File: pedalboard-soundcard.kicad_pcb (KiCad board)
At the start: 2 copper layers, 65 x 56 mm, 76 parts, among them J1 RPi_GPIO, J2 Conn_02x03_Odd_Even, J3 Conn_02x03_Odd_Even, U1 AT24CS01-STUM, U2 NCP163, U3 NCP163, U4 PCM1863DBT, U5 NCP163, U6 PCM5242RHBR, X1 22.5792Mhz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

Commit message: Replace 5v global label with +5V power
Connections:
- net 5v renamed +5V
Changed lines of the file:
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@@
   (net 18 "unconnected-(J1-BCM24-Pad18)")
   (net 19 "unconnected-(J1-BCM10_MOSI-Pad19)")
-  (net 20 "5v")
+  (net 20 "+5V")
   (net 21 "unconnected-(J1-BCM9_MISO-Pad21)")
   (net 22 "unconnected-(J1-BCM25-Pad22)")
@@
       (net 1 "unconnected-(J1-3.3V-Pad1)") (pinfunction "3.3V") (pintype "power_in+no_connect"))
     (pad "2" thru_hole oval locked (at 1.27 -24.13 90) (size 1.7272 1.7272) (drill 1.016) (layers "*.Cu" "*.Mask")
-      (net 20 "5v") (pinfunction "5V") (pintype "power_in"))
+      (net 20 "+5V") (pinfunction "5V") (pintype "power_in"))
     (pad "3" thru_hole oval locked (at -1.27 -21.59 90) (size 1.7272 1.7272) (drill 1.016) (layers "*.Cu" "*.Mask")
       (net 47 "sda") (pinfunction "BCM2_SDA") (pintype "bidirectional"))
     (pad "4" thru_hole oval locked (at 1.27 -21.59 90) (size 1.7272 1.7272) (drill 1.016) (layers "*.Cu" "*.Mask")
-      (net 20 "5v") (pinfunction "5V") (pintype "power_in"))
+      (net 20 "+5V") (pinfunction "5V") (pintype "power_in"))
     (pad "5" thru_hole oval locked (at -1.27 -19.05 90) (size 1.7272 1.7272) (drill 1.016) (layers "*.Cu" "*.Mask")
       (net 48 "scl") (pinfunction "BCM3_SCL") (pintype "bidirectional"))
@@
       (stroke (width 0.1) (type solid)) (layer "F.Fab"))
     (pad "1" smd roundrect (at -1.1375 -0.95 270) (size 1.325 0.6) (layers "F.Cu" "F.Paste" "F.Mask") (roundrect_rratio 0.25)
-      (net 20 "5v") (pinfunction "IN") (pintype "power_in"))
+      (net 20 "+5V") (pinfunction "IN") (pintype "power_in"))
     (pad "2" smd roundrect (at -1.1375 0 270) (size 1.325 0.6) (layers "F.Cu" "F.Paste" "F.Mask") (roundrect_rratio 0.25)
       (net 2 "GND") (pinfunction "GND") (pintype "power_in"))
     (pad "3" smd roundrect (at -1.1375 0.95 270) (size 1.325 0.6) (layers "F.Cu" "F.Paste" "F.Mask") (roundrect_rratio 0.25)
-      (net 20 "5v") (pinfunction "EN") (pintype "input"))
+      (net 20 "+5V") (pinfunction "EN") (pintype "input"))
     (pad "4" smd roundrect (at 1.1375 0.95 270) (size 1.325 0.6) (layers "F.Cu" "F.Paste" "F.Mask") (roundrect_rratio 0.25)
       (net 76 "unconnected-(U2-NC-Pad4)") (pinfunction "NC") (pintype "no_connect"))
@@
       (stroke (width 0.1) (type solid)) (layer "F.Fab"))
     (pad "1" smd roundrect (at -0.95 0 180) (size 1 1.45) (layers "F.Cu" "F.Paste" "F.Mask") (roundrect_rratio 0.25)
-      (net 20 "5v") (pintype "passive"))
+      (net 20 "+5V") (pintype "passive"))
     (pad "2" smd roundrect (at 0.95 0 180) (size 1 1.45) (layers "F.Cu" "F.Paste" "F.Mask") (roundrect_rratio 0.25)
       (net 2 "GND") (pintype "passive"))
@@
       (stroke (width 0.1) (type solid)) (layer "F.Fab"))
     (pad "1" smd roundrect (at -1.1375 -0.95 270) (size 1.325 0.6) (layers "F.Cu" "F.Paste" "F.Mask") (roundrect_rratio 0.25)
-      (net 20 "5v") (pinfunction "IN") (pintype "power_in"))
+      (net 20 "+5V") (pinfunction "IN") (pintype "power_in"))
     (pad "2" smd roundrect (at -1.1375 0 270) (size 1.325 0.6) (layers "F.Cu" "F.Paste" "F.Mask") (roundrect_rratio 0.25)
       (net 2 "GND") (pinfunction "GND") (pintype "power_in"))
     (pad "3" smd roundrect (at -1.1375 0.95 270) (size 1.325 0.6) (layers "F.Cu" "F.Paste" "F.Mask") (roundrect_rratio 0.25)
-      (net 20 "5v") (pinfunction "EN") (pintype "input"))
+      (net 20 "+5V") (pinfunction "EN") (pintype "input"))
     (pad "4" smd roundrect (at 1.1375 0.95 270) (size 1.325 0.6) (layers "F.Cu" "F.Paste" "F.Mask") (roundrect_rratio 0.25)
       (net 78 "unconnected-(U5-NC-Pad4)") (pinfunction "NC") (pintype "no_connect"))
@@
       (stroke (width 0.1) (type solid)) (layer "F.Fab"))
     (pad "1" smd roundrect (at -0.95 0 180) (size 1 1.45) (layers "F.Cu" "F.Paste" "F.Mask") (roundrect_rratio 0.25)
-      (net 20 "5v") (pintype "passive"))
+      (net 20 "+5V") (pintype "passive"))
     (pad "2" smd roundrect (at 0.95 0 180) (size 1 1.45) (layers "F.Cu" "F.Paste" "F.Mask") (roundrect_rratio 0.25)
       (net 2 "GND") (pintype "passive"))
@@
       (stroke (width 0.1) (type solid)) (layer "F.Fab"))
     (pad "1" smd roundrect (at -1.1375 -0.95 270) (size 1.325 0.6) (layers "F.Cu" "F.Paste" "F.Mask") (roundrect_rratio 0.25)
-      (net 20 "5v") (pinfunction "IN") (pintype "power_in"))
+      (net 20 "+5V") (pinfunction "IN") (pintype "power_in"))
     (pad "2" smd roundrect (at -1.1375 0 270) (size 1.325 0.6) (layers "F.Cu" "F.Paste" "F.Mask") (roundrect_rratio 0.25)
       (net 2 "GND") (pinfunction "GND") (pintype "power_in"))
     (pad "3" smd roundrect (at -1.1375 0.95 270) (size 1.325 0.6) (layers "F.Cu" "F.Paste" "F.Mask") (roundrect_rratio 0.25)
-      (net 20 "5v") (pinfunction "EN") (pintype "input"))
+      (net 20 "+5V") (pinfunction "EN") (pintype "input"))
     (pad "4" smd roundrect (at 1.1375 0.95 270) (size 1.325 0.6) (layers "F.Cu" "F.Paste" "F.Mask") (roundrect_rratio 0.25)
       (net 77 "unconnected-(U3-NC-Pad4)") (pinfunction "NC") (pintype "no_connect"))
@@
       (stroke (width 0.1) (type solid)) (layer "F.Fab"))
     (pad "1" smd roundrect (at -0.95 0) (size 1 1.45) (layers "F.Cu" "F.Paste" "F.Mask") (roundrect_rratio 0.25)
-      (net 20 "5v") (pintype "passive"))
+      (net 20 "+5V") (pintype "passive"))
     (pad "2" smd roundrect (at 0.95 0) (size 1 1.45) (layers "F.Cu" "F.Paste" "F.Mask") (roundrect_rratio 0.25)
       (net 2 "GND") (pintype "passive"))

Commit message: Replace DVDD global label with VDD power symbol
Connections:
- net DVDD renamed VDD
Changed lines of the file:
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@@
   (net 1 "unconnected-(J1-3.3V-Pad1)")
   (net 2 "GND")
-  (net 3 "DVDD")
+  (net 3 "VDD")
   (net 4 "Net-(C2-Pad1)")
   (net 5 "/ADC/inr+")
@@
       (net 73 "Net-(X1-OUT)") (pinfunction "OUT") (pintype "output"))
     (pad "4" smd rect (at -0.825 -0.775 90) (size 0.65 0.85) (layers "F.Cu" "F.Paste" "F.Mask")
-      (net 3 "DVDD") (pinfunction "VDD") (pintype "power_in"))
+      (net 3 "VDD") (pinfunction "VDD") (pintype "power_in"))
     (model "${KICAD6_3DMODEL_DIR}/Oscillator.3dshapes/Oscillator_SMD_Abracon_ASDMB-4Pin_2.5x2.0mm.wrl"
       (offset (xyz 0 0 0))
@@
       (net 76 "unconnected-(U2-NC-Pad4)") (pinfunction "NC") (pintype "no_connect"))
     (pad "5" smd roundrect (at 1.1375 -0.95 270) (size 1.325 0.6) (layers "F.Cu" "F.Paste" "F.Mask") (roundrect_rratio 0.25)
-      (net 3 "DVDD") (pinfunction "OUT") (pintype "power_out"))
+      (net 3 "VDD") (pinfunction "OUT") (pintype "power_out"))
     (model "${KICAD6_3DMODEL_DIR}/Package_TO_SOT_SMD.3dshapes/SOT-23-5.wrl"
       (offset (xyz 0 0 0))
@@
       (stroke (width 0.1) (type solid)) (layer "F.Fab"))
     (pad "1" smd roundrect (at -0.95 0 90) (size 1 1.45) (layers "F.Cu" "F.Paste" "F.Mask") (roundrect_rratio 0.25)
-      (net 3 "DVDD") (pintype "passive"))
+      (net 3 "VDD") (pintype "passive"))
     (pad "2" smd roundrect (at 0.95 0 90) (size 1 1.45) (layers "F.Cu" "F.Paste" "F.Mask") (roundrect_rratio 0.25)
       (net 2 "GND") (pintype "passive"))
@@
       (stroke (width 0.1) (type solid)) (layer "F.Fab"))
     (pad "1" smd roundrect (at -0.95 0) (size 1 1.45) (layers "F.Cu" "F.Paste" "F.Mask") (roundrect_rratio 0.25)
-      (net 3 "DVDD") (pintype "passive"))
+      (net 3 "VDD") (pintype "passive"))
     (pad "2" smd roundrect (at 0.95 0) (size 1 1.45) (layers "F.Cu" "F.Paste" "F.Mask") (roundrect_rratio 0.25)
       (net 2 "GND") (pintype "passive"))
@@
       (net 51 "/ID_SC") (pintype "passive"))
     (pad "2" smd roundrect (at 0.9125 0) (size 1.025 1.4) (layers "F.Cu" "F.Paste" "F.Mask") (roundrect_rratio 0.243902)
-      (net 3 "DVDD") (pintype "passive"))
+      (net 3 "VDD") (pintype "passive"))
     (model "${KICAD6_3DMODEL_DIR}/Resistor_SMD.3dshapes/R_0805_2012Metric.wrl"
       (offset (xyz 0 0 0))
@@
       (stroke (width 0.1) (type solid)) (layer "F.Fab"))
     (pad "1" smd roundrect (at -0.9125 0) (size 1.025 1.4) (layers "F.Cu" "F.Paste" "F.Mask") (roundrect_rratio 0.243902)
-      (net 3 "DVDD") (pintype "passive"))
+      (net 3 "VDD") (pintype "passive"))
     (pad "2" smd roundrect (at 0.9125 0) (size 1.025 1.4) (layers "F.Cu" "F.Paste" "F.Mask") (roundrect_rratio 0.243902)
       (net 58 "Net-(U1-WP)") (pintype "passive"))
@@
       (net 75 "Net-(X2-OUT)") (pinfunction "OUT") (pintype "output"))
     (pad "4" smd rect (at -0.825 -0.775 90) (size 0.65 0.85) (layers "F.Cu" "F.Paste" "F.Mask")
-      (net 3 "DVDD") (pinfunction "VDD") (pintype "power_in"))
+      (net 3 "VDD") (pinfunction "VDD") (pintype "power_in"))
     (model "${KICAD6_3DMODEL_DIR}/Oscillator.3dshapes/Oscillator_SMD_Abracon_ASDMB-4Pin_2.5x2.0mm.wrl"
       (offset (xyz 0 0 0))
@@
       (net 2 "GND") (pintype "passive"))
     (pad "2" smd roundrect (at 0.95 0 90) (size 1 1.45) (layers "F.Cu" "F.Paste" "F.Mask") (roundrect_rratio 0.25)
-      (net 3 "DVDD") (pintype "passive"))
+      (net 3 "VDD") (pintype "passive"))
     (model "${KICAD6_3DMODEL_DIR}/Capacitor_SMD.3dshapes/C_0805_2012Metric.wrl"
       (offset (xyz 0 0 0))
@@
       (stroke (width 0.1) (type solid)) (layer "F.Fab"))
     (pad "1" smd roundrect (at -0.95 0 180) (size 1 1.45) (layers "F.Cu" "F.Paste" "F.Mask") (roundrect_rratio 0.25)
-      (net 3 "DVDD") (pintype "passive"))
+      (net 3 "VDD") (pintype "passive"))
     (pad "2" smd roundrect (at 0.95 0 180) (size 1 1.45) (layers "F.Cu" "F.Paste" "F.Mask") (roundrect_rratio 0.25)
       (net 2 "GND") (pintype "passive"))
@@
       (net 2 "GND") (pinfunction "DGND") (pintype "power_in"))
     (pad "4" smd roundrect (at -2.4375 -0.25 90) (size 0.875 0.25) (layers "F.Cu" "F.Paste" "F.Mask") (roundrect_rratio 0.25)
-      (net 3 "DVDD") (pinfunction "DVDD") (pintype "power_in"))
+      (net 3 "VDD") (pinfunction "DVDD") (pintype "power_in"))
     (pad "5" smd roundrect (at -2.4375 0.25 90) (size 0.875 0.25) (layers "F.Cu" "F.Paste" "F.Mask") (roundrect_rratio 0.25)
-      (net 3 "DVDD") (pinfunction "CPVDD") (pintype "power_in"))
+      (net 3 "VDD") (pinfunction "CPVDD") (pintype "power_in"))
     (pad "6" smd roundrect (at -2.4375 0.75 90) (size 0.875 0.25) (layers "F.Cu" "F.Paste" "F.Mask") (roundrect_rratio 0.25)
       (net 46 "Net-(U6-CAPP)") (pinfunction "CAPP") (pintype "output"))
@@
       (net 2 "GND") (pinfunction "DGND") (pintype "power_in"))
     (pad "13" smd roundrect (at -2.8625 2.5 180) (size 1.475 0.3) (layers "F.Cu" "F.Paste" "F.Mask") (roundrect_rratio 0.25)
-      (net 3 "DVDD") (pinfunction "DVDD") (pintype "power_in"))
+      (net 3 "VDD") (pinfunction "DVDD") (pintype "power_in"))
     (pad "14" smd roundrect (at -2.8625 3 180) (size 1.475 0.3) (layers "F.Cu" "F.Paste" "F.Mask") (roundrect_rratio 0.25)
-      (net 3 "DVDD") (pinfunction "IOVDD") (pintype "power_in"))
+      (net 3 "VDD") (pinfunction "IOVDD") (pintype "power_in"))
     (pad "15" smd roundrect (at -2.8625 3.5 180) (size 1.475 0.3) (layers "F.Cu" "F.Paste" "F.Mask") (roundrect_rratio 0.25)
       (net 74 "master_clk") (pinfunction "SCKI") (pintype "input"))
@@
       (net 2 "GND") (pintype "passive"))
     (pad "2" smd roundrect (at 0.95 0 90) (size 1 1.45) (layers "F.Cu" "F.Paste" "F.Mask") (roundrect_rratio 0.25)
-      (net 3 "DVDD") (pintype "passive"))
+      (net 3 "VDD") (pintype "passive"))
     (model "${KICAD6_3DMODEL_DIR}/Capacitor_SMD.3dshapes/C_0805_2012Metric.wrl"
       (offset (xyz 0 0 0))
@@
       (net 2 "GND") (pintype "passive"))
     (pad "2" smd roundrect (at 0.95 0 90) (size 1 1.45) (layers "F.Cu" "F.Paste" "F.Mask") (roundrect_rratio 0.25)
-      (net 3 "DVDD") (pintype "passive"))
+      (net 3 "VDD") (pintype "passive"))
     (model "${KICAD6_3DMODEL_DIR}/Capacitor_SMD.3dshapes/C_0805_2012Metric.wrl"
       (offset (xyz 0 0 0))
@@
       (net 67 "Net-(U6-ADR1)") (pintype "passive"))
     (pad "2" smd roundrect (at 0.9125 0 180) (size 1.025 1.4) (layers "F.Cu" "F.Paste" "F.Mask") (roundrect_rratio 0.243902)
-      (net 3 "DVDD") (pintype "passive"))
+      (net 3 "VDD") (pintype "passive"))
     (model "${KICAD6_3DMODEL_DIR}/Resistor_SMD.3dshapes/R_0805_2012Metric.wrl"
       (offset (xyz 0 0 0))
@@
       (net 50 "/ID_SD") (pintype "passive"))
     (pad "2" smd roundrect (at 0.9125 0) (size 1.025 1.4) (layers "F.Cu" "F.Paste" "F.Mask") (roundrect_rratio 0.243902)
-      (net 3 "DVDD") (pintype "passive"))
+      (net 3 "VDD") (pintype "passive"))
     (model "${KICAD6_3DMODEL_DIR}/Resistor_SMD.3dshapes/R_0805_2012Metric.wrl"
       (offset (xyz 0 0 0))
@@
       (net 50 "/ID_SD") (pinfunction "SDA") (pintype "bidirectional"))
     (pad "4" smd roundrect (at 1.1375 0.95 180) (size 1.325 0.6) (layers "F.Cu" "F.Paste" "F.Mask") (roundrect_rratio 0.25)
-      (net 3 "DVDD") (pinfunction "VCC") (pintype "power_in"))
+      (net 3 "VDD") (pinfunction "VCC") (pintype "power_in"))
     (pad "5" smd roundrect (at 1.1375 -0.95 180) (size 1.325 0.6) (layers "F.Cu" "F.Paste" "F.Mask") (roundrect_rratio 0.25)
       (net 58 "Net-(U1-WP)") (pinfunction "WP") (pintype "input"))
@@
       (stroke (width 0.1) (type solid)) (layer "F.Fab"))
     (pad "1" smd roundrect (at -0.95 0 90) (size 1 1.45) (layers "F.Cu" "F.Paste" "F.Mask") (roundrect_rratio 0.25)
-      (net 3 "DVDD") (pintype "passive"))
+      (net 3 "VDD") (pintype "passive"))
     (pad "2" smd roundrect (at 0.95 0 90) (size 1 1.45) (layers "F.Cu" "F.Paste" "F.Mask") (roundrect_rratio 0.25)
       (net 2 "GND") (pintype "passive"))

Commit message: Use Power Symbols for analog power
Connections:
- net AVDD renamed VDDA
- net AVDD2 renamed VDDF
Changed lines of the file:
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@@
   (net 26 "unconnected-(J1-BCM7_CE1-Pad26)")
   (net 27 "/ADC/inl+")
-  (net 28 "AVDD2")
+  (net 28 "VDDF")
   (net 29 "unconnected-(J1-BCM5-Pad29)")
   (net 30 "Net-(U4-LDO)")
@@
   (net 32 "unconnected-(J1-BCM12_PWM0-Pad32)")
   (net 33 "unconnected-(J1-BCM13_PWM1-Pad33)")
-  (net 34 "AVDD")
+  (net 34 "VDDA")
   (net 35 "Net-(U4-VREF)")
   (net 36 "unconnected-(J1-BCM16-Pad36)")
@@
       (stroke (width 0.1) (type solid)) (layer "F.Fab"))
     (pad "1" smd roundrect (at -0.95 0) (size 1 1.45) (layers "F.Cu" "F.Paste" "F.Mask") (roundrect_rratio 0.25)
-      (net 28 "AVDD2") (pintype "passive"))
+      (net 28 "VDDF") (pintype "passive"))
     (pad "2" smd roundrect (at 0.95 0) (size 1 1.45) (layers "F.Cu" "F.Paste" "F.Mask") (roundrect_rratio 0.25)
       (net 2 "GND") (pintype "passive"))
@@
       (net 2 "GND") (pintype "passive"))
     (pad "2" smd roundrect (at 0.95 0 180) (size 1 1.45) (layers "F.Cu" "F.Paste" "F.Mask") (roundrect_rratio 0.25)
-      (net 34 "AVDD") (pintype "passive"))
+      (net 34 "VDDA") (pintype "passive"))
     (model "${KICAD6_3DMODEL_DIR}/Capacitor_SMD.3dshapes/C_0805_2012Metric.wrl"
       (offset (xyz 0 0 0))
@@
       (net 66 "Net-(U6-OUTRP)") (pinfunction "OUTRP") (pintype "output"))
     (pad "14" smd roundrect (at 0.75 2.4375 90) (size 0.25 0.875) (layers "F.Cu" "F.Paste" "F.Mask") (roundrect_rratio 0.25)
-      (net 34 "AVDD") (pinfunction "AVDD") (pintype "power_in"))
+      (net 34 "VDDA") (pinfunction "AVDD") (pintype "power_in"))
     (pad "15" smd roundrect (at 1.25 2.4375 90) (size 0.25 0.875) (layers "F.Cu" "F.Paste" "F.Mask") (roundrect_rratio 0.25)
       (net 2 "GND") (pinfunction "AGND") (pintype "power_in"))
@@
       (net 78 "unconnected-(U5-NC-Pad4)") (pinfunction "NC") (pintype "no_connect"))
     (pad "5" smd roundrect (at 1.1375 -0.95 270) (size 1.325 0.6) (layers "F.Cu" "F.Paste" "F.Mask") (roundrect_rratio 0.25)
-      (net 34 "AVDD") (pinfunction "OUT") (pintype "power_out"))
+      (net 34 "VDDA") (pinfunction "OUT") (pintype "power_out"))
     (model "${KICAD6_3DMODEL_DIR}/Package_TO_SOT_SMD.3dshapes/SOT-23-5.wrl"
       (offset (xyz 0 0 0))
@@
       (stroke (width 0.1) (type solid)) (layer "F.Fab"))
     (pad "1" smd roundrect (at -0.95 0) (size 1 1.45) (layers "F.Cu" "F.Paste" "F.Mask") (roundrect_rratio 0.25)
-      (net 34 "AVDD") (pintype "passive"))
+      (net 34 "VDDA") (pintype "passive"))
     (pad "2" smd roundrect (at 0.95 0) (size 1 1.45) (layers "F.Cu" "F.Paste" "F.Mask") (roundrect_rratio 0.25)
       (net 2 "GND") (pintype "passive"))
@@
       (stroke (width 0.1) (type solid)) (layer "F.Fab"))
     (pad "1" smd roundrect (at -0.95 0) (size 1 1.45) (layers "F.Cu" "F.Paste" "F.Mask") (roundrect_rratio 0.25)
-      (net 34 "AVDD") (pintype "passive"))
+      (net 34 "VDDA") (pintype "passive"))
     (pad "2" smd roundrect (at 0.95 0) (size 1 1.45) (layers "F.Cu" "F.Paste" "F.Mask") (roundrect_rratio 0.25)
       (net 2 "GND") (pintype "passive"))
@@
       (net 2 "GND") (pinfunction "AGND") (pintype "power_in"))
     (pad "8" smd roundrect (at -2.8625 0 180) (size 1.475 0.3) (layers "F.Cu" "F.Paste" "F.Mask") (roundrect_rratio 0.25)
-      (net 28 "AVDD2") (pinfunction "AVDD") (pintype "power_in"))
+      (net 28 "VDDF") (pinfunction "AVDD") (pintype "power_in"))
     (pad "9" smd roundrect (at -2.8625 0.5 180) (size 1.475 0.3) (layers "F.Cu" "F.Paste" "F.Mask") (roundrect_rratio 0.25)
       (net 79 "unconnected-(U4-XO-Pad9)") (pinfunction "XO") (pintype "output+no_connect"))
@@
       (net 77 "unconnected-(U3-NC-Pad4)") (pinfunction "NC") (pintype "no_connect"))
     (pad "5" smd roundrect (at 1.1375 -0.95 270) (size 1.325 0.6) (layers "F.Cu" "F.Paste" "F.Mask") (roundrect_rratio 0.25)
-      (net 28 "AVDD2") (pinfunction "OUT") (pintype "power_out"))
+      (net 28 "VDDF") (pinfunction "OUT") (pintype "power_out"))
     (model "${KICAD6_3DMODEL_DIR}/Package_TO_SOT_SMD.3dshapes/SOT-23-5.wrl"
       (offset (xyz 0 0 0))
@@
       (stroke (width 0.1) (type solid)) (layer "F.Fab"))
     (pad "1" smd roundrect (at -0.95 0) (size 1 1.45) (layers "F.Cu" "F.Paste" "F.Mask") (roundrect_rratio 0.25)
-      (net 28 "AVDD2") (pintype "passive"))
+      (net 28 "VDDF") (pintype "passive"))
     (pad "2" smd roundrect (at 0.95 0) (size 1 1.45) (layers "F.Cu" "F.Paste" "F.Mask") (roundrect_rratio 0.25)
       (net 2 "GND") (pintype "passive"))
@@
       (stroke (width 0.1) (type solid)) (layer "F.Fab"))
     (pad "1" smd roundrect (at -0.95 0) (size 1 1.45) (layers "F.Cu" "F.Paste" "F.Mask") (roundrect_rratio 0.25)
-      (net 28 "AVDD2") (pintype "passive"))
+      (net 28 "VDDF") (pintype "passive"))
     (pad "2" smd roundrect (at 0.95 0) (size 1 1.45) (layers "F.Cu" "F.Paste" "F.Mask") (roundrect_rratio 0.25)
       (net 2 "GND") (pintype "passive"))

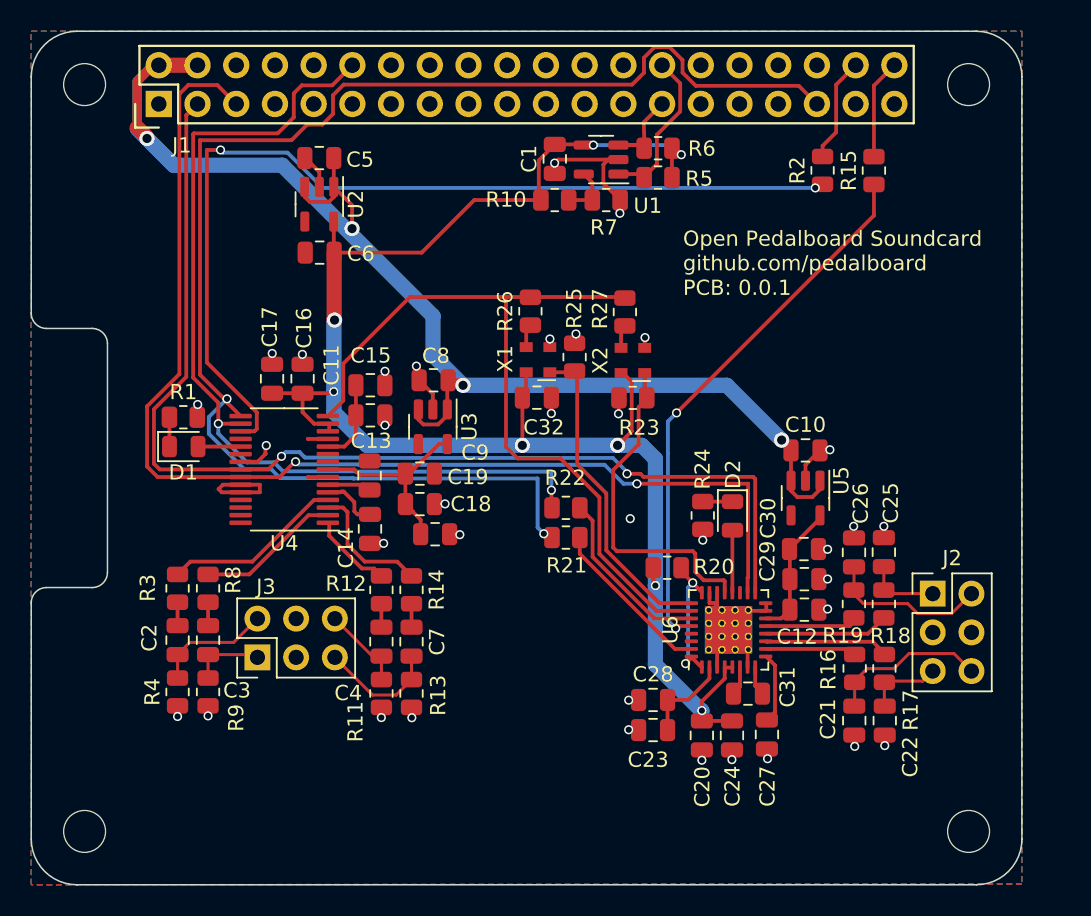
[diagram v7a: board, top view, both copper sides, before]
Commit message: Add Fiducials and OSHW logo
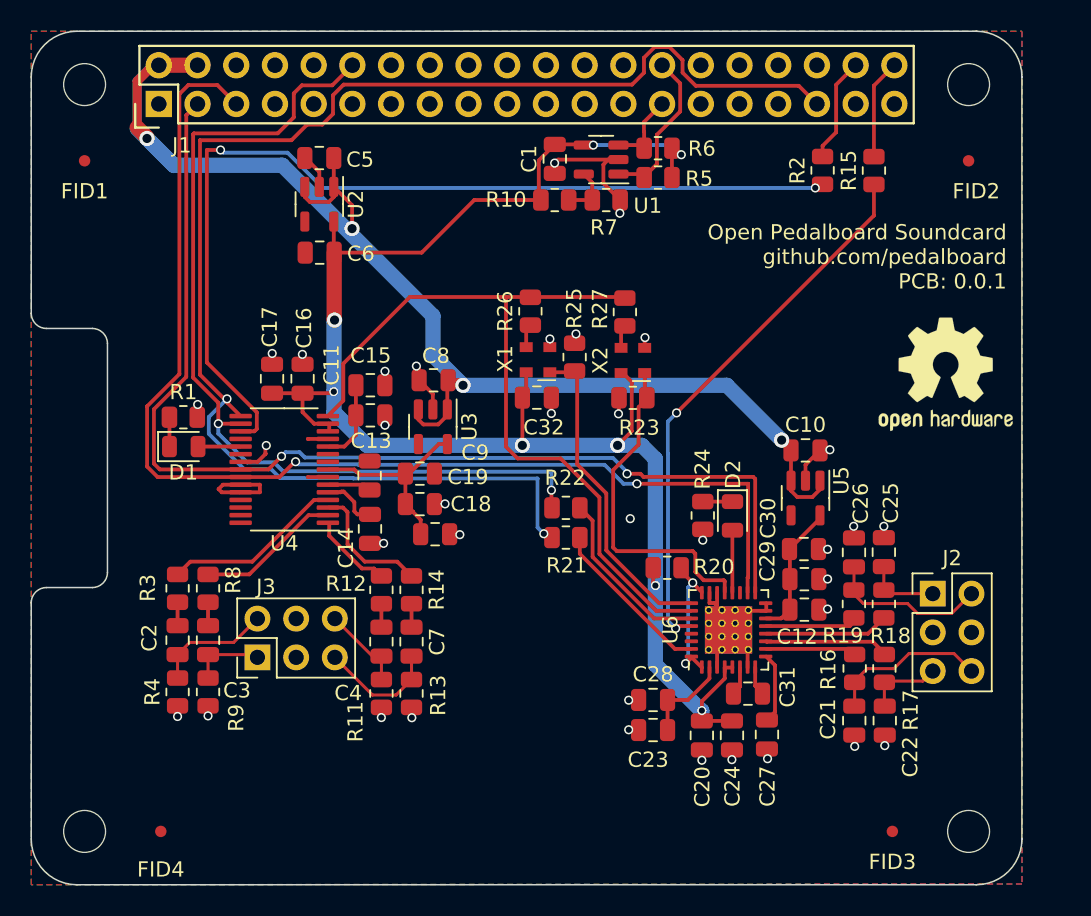
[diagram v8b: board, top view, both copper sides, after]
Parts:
- added FID1: Fiducial, Fiducial:Fiducial_0.75mm_Mask1.5mm, F.Cu at (52.0, 61.0)
- added FID2: Fiducial, Fiducial:Fiducial_0.75mm_Mask1.5mm, F.Cu at (110.0, 61.0)
- added FID3: Fiducial, Fiducial:Fiducial_0.75mm_Mask1.5mm, F.Cu at (105.0, 105.0)
- added FID4: Fiducial, Fiducial:Fiducial_0.75mm_Mask1.5mm, F.Cu at (57.0, 105.0)
- added SYM1: Logo_Open_Hardware_Small, Symbol:OSHW-Logo2_9.8x8mm_SilkScreen, F.Cu at (108.5, 75.0)
